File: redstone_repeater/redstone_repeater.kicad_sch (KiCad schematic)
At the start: 41 parts, among them J1 1x4_Pogo, J2 1x4_Pogo, J3 1x4_Pogo, J4 1x4_Pogo, J5 1x4_Pogo, J6 1x4_Pogo, J7 1x4_Pogo, J8 1x4_Pogo, J9 2.54mm_ProgrammingPin, Q1 BC108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

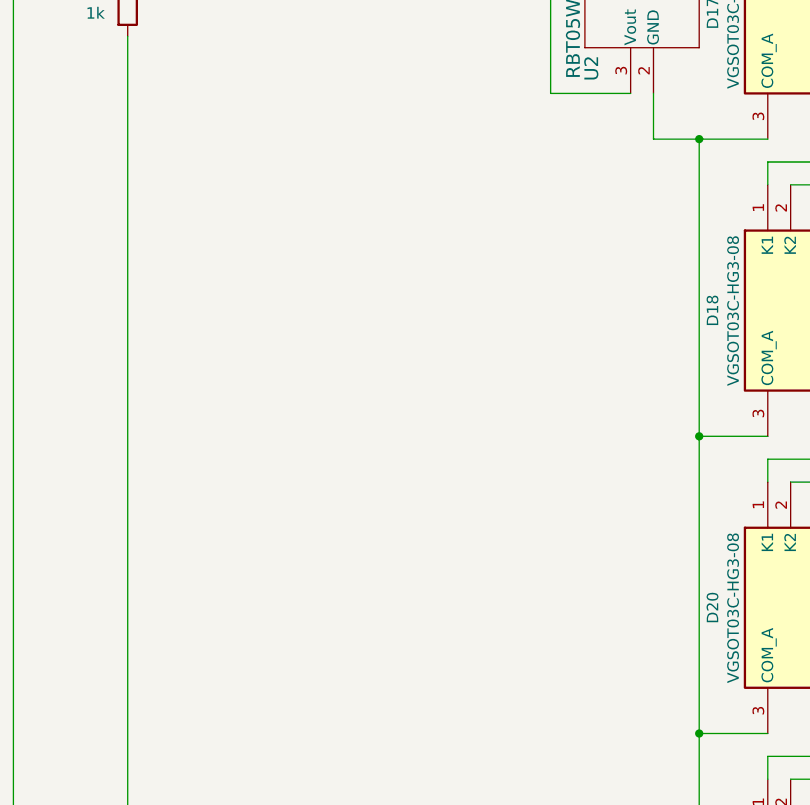
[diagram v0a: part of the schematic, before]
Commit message: add 4 way switch for repeater
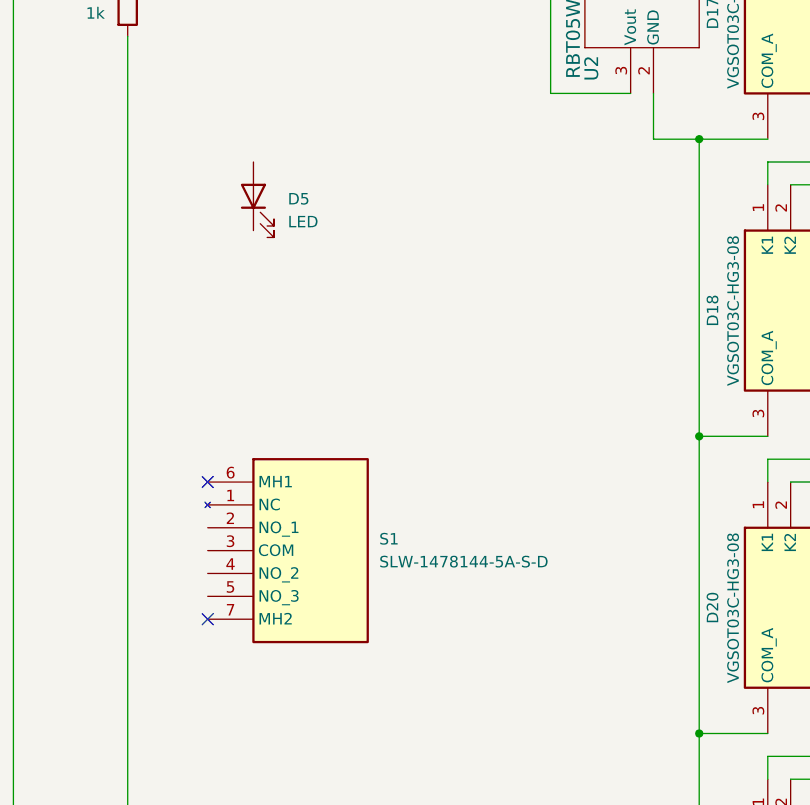
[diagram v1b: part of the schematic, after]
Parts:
- added D5: LED, LED_THT:LED_D3.0mm, symbol Device:LED
- added S1: SLW-1478144-5A-S-D, SLW14781445ASD, symbol SamacSys_Parts:SLW-1478144-5A-S-D
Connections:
- no-connect marks 34 -> 36
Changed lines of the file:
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@@
 	)
 	(no_connect
+		(at 187.96 100.33)
+	)
+	(no_connect
+		(at 187.96 115.57)
+	)
+	(no_connect
 		(at 128.27 157.48)
 	)
@@
 	)
 	(symbol
+		(lib_id "SamacSys_Parts:SLW-1478144-5A-S-D")
+		(at 187.96 100.33 0)
+		(unit 1)
+		(exclude_from_sim no)
+		(in_bom yes)
+		(on_board yes)
+		(dnp no)
+		(fields_autoplaced yes)
+		(property "Reference" "S1"
+			(at 207.01 106.6799 0)
+			(effects
+				(font
+					(size 1.27 1.27)
+				)
+				(justify left)
+			)
+		)
+		(property "Value" "SLW-1478144-5A-S-D"
+			(at 207.01 109.2199 0)
+			(effects
+				(font
+					(size 1.27 1.27)
+				)
+				(justify left)
+			)
+		)
+		(property "Footprint" "SLW14781445ASD"
+			(at 207.01 195.25 0)
+			(effects
+				(font
+					(size 1.27 1.27)
+				)
+				(justify left top)
+				(hide yes)
+			)
+		)
+		(property "Datasheet" "https://www.sameskydevices.com/product/resource/supplyframepdf/slw-1478144-5a-s-d.pdf"
+			(at 207.01 295.25 0)
+			(effects
+				(font
+					(size 1.27 1.27)
+				)
+				(justify left top)
+				(hide yes)
+			)
+		)
+		(property "Description" "14.7 x 8.1 x 4.4 mm, 5 mm Raised Slide Actuator, Through Hole, Slide Switch"
+			(at 187.96 100.33 0)
+			(effects
+				(font
+					(size 1.27 1.27)
+				)
+				(hide yes)
+			)
+		)
+		(property "Height" "10"
+			(at 207.01 495.25 0)
+			(effects
+				(font
+					(size 1.27 1.27)
+				)
+				(justify left top)
+				(hide yes)
+			)
+		)
+		(property "Manufacturer_Name" "Same Sky"
+			(at 207.01 595.25 0)
+			(effects
+				(font
+					(size 1.27 1.27)
+				)
+				(justify left top)
+				(hide yes)
+			)
+		)
+		(property "Manufacturer_Part_Number" "SLW-1478144-5A-S-D"
+			(at 207.01 695.25 0)
+			(effects
+				(font
+					(size 1.27 1.27)
+				)
+				(justify left top)
+				(hide yes)
+			)
+		)
+		(property "Mouser Part Number" ""
+			(at 207.01 795.25 0)
+			(effects
+				(font
+					(size 1.27 1.27)
+				)
+				(justify left top)
+				(hide yes)
+			)
+		)
+		(property "Mouser Price/Stock" ""
+			(at 207.01 895.25 0)
+			(effects
+				(font
+					(size 1.27 1.27)
+				)
+				(justify left top)
+				(hide yes)
+			)
+		)
+		(property "Arrow Part Number" ""
+			(at 207.01 995.25 0)
+			(effects
+				(font
+					(size 1.27 1.27)
+				)
+				(justify left top)
+				(hide yes)
+			)
+		)
+		(property "Arrow Price/Stock" ""
+			(at 207.01 1095.25 0)
+			(effects
+				(font
+					(size 1.27 1.27)
+				)
+				(justify left top)
+				(hide yes)
+			)
+		)
+		(pin "6"
+		)
+		(pin "2"
+		)
+		(pin "1"
+		)
+		(pin "4"
+		)
+		(pin "3"
+		)
+		(pin "7"
+		)
+		(pin "5"
+		)
+		(instances
+			(project ""
+				(path "/bc70a981-f687-4b66-9b14-62168cfa8164"
+					(reference "S1")
+					(unit 1)
+				)
+			)
+		)
+	)
+	(symbol
 		(lib_id "Connector_Generic_MountingPin:Conn_01x04_MountingPin")
 		(at 270.51 85.09 0)
@@
 					(unit 1)
 				)
+			)
+		)
+	)
+	(symbol
+		(lib_id "Device:LED")
+		(at 193.04 68.58 90)
+		(unit 1)
+		(exclude_from_sim no)
+		(in_bom yes)
+		(on_board yes)
+		(dnp no)
+		(fields_autoplaced yes)
+		(property "Reference" "D5"
+			(at 196.85 68.8974 90)
+			(effects
+				(font
+					(size 1.27 1.27)
+				)
+				(justify right)
+			)
+		)
+		(property "Value" "LED"
+			(at 196.85 71.4374 90)
+			(effects
+				(font
+					(size 1.27 1.27)
+				)
+				(justify right)
+			)
+		)
+		(property "Footprint" "LED_THT:LED_D3.0mm"
+			(at 193.04 68.58 0)
+			(effects
+				(font
+					(size 1.27 1.27)
+				)
+				(hide yes)
+			)
+		)
+		(property "Datasheet" "~"
+			(at 193.04 68.58 0)
+			(effects
+				(font
+					(size 1.27 1.27)
+				)
+				(hide yes)
+			)
+		)
+		(property "Description" "Light emitting diode"
+			(at 193.04 68.58 0)
+			(effects
+				(font
+					(size 1.27 1.27)
+				)
+				(hide yes)
+			)
+		)
+		(property "Sim.Pins" "1=K 2=A"
+			(at 193.04 68.58 0)
+			(effects
+				(font
+					(size 1.27 1.27)
+				)
+				(hide yes)
+			)
+		)
+		(pin "2"
+		)
+		(pin "1"
+		)
+		(instances
+			(project ""
+				(path "/bc70a981-f687-4b66-9b14-62168cfa8164"
+					(reference "D5")
+					(unit 1)
+				)

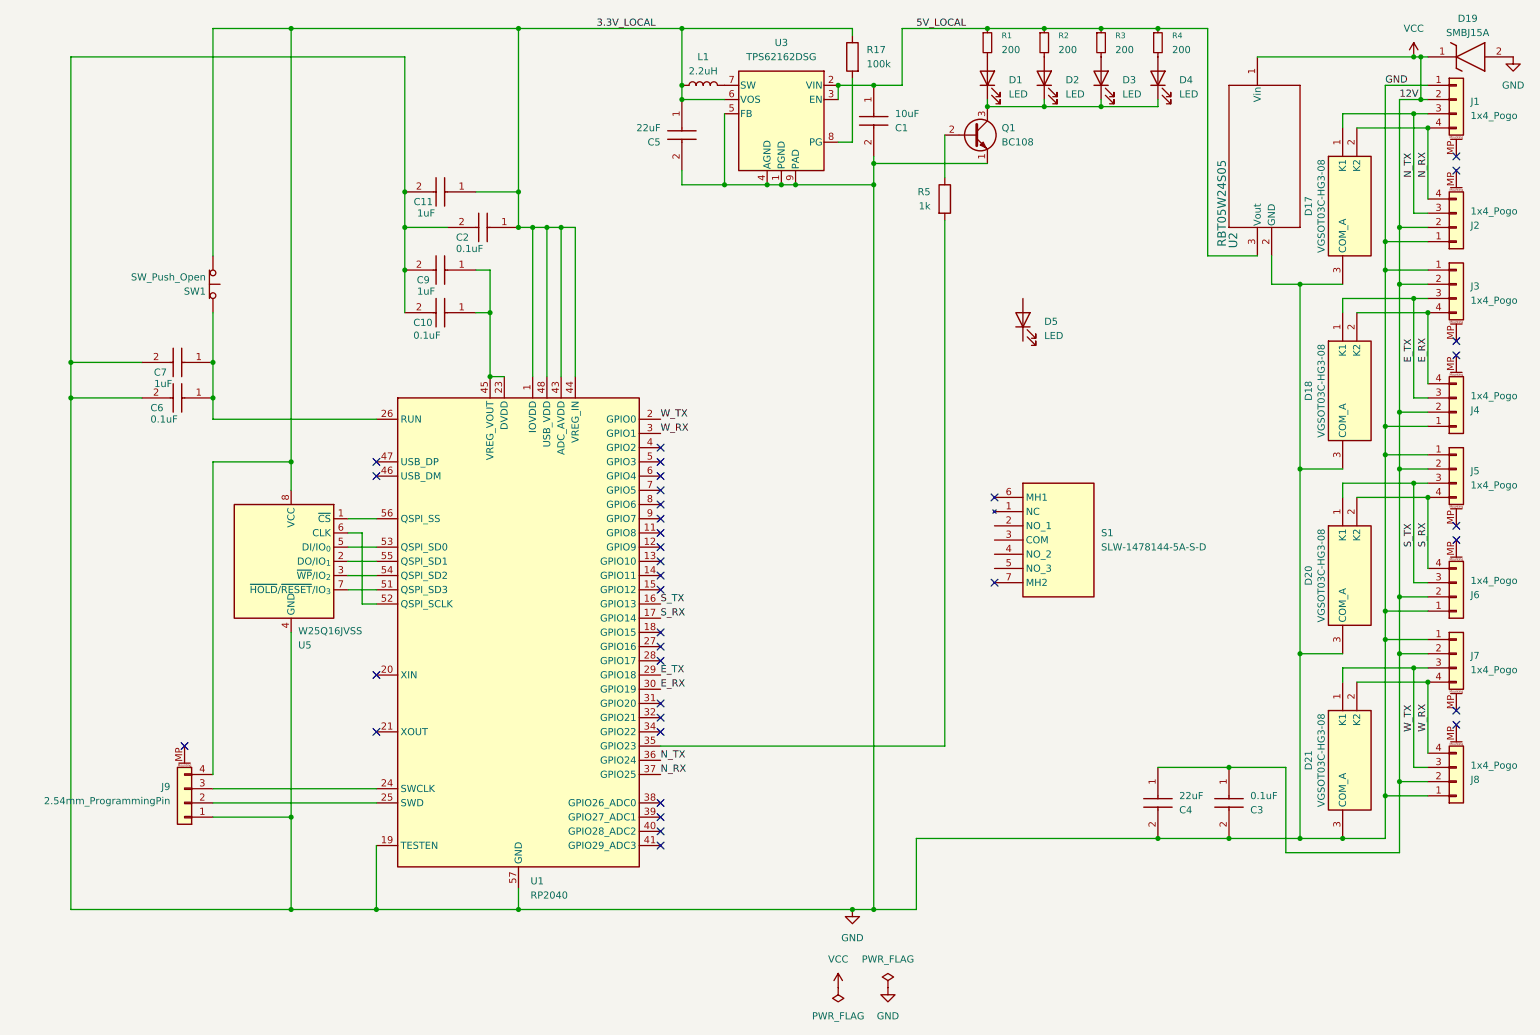
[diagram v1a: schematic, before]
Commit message: add four individually controlled leds for repeater, small adjustments for redstone dust
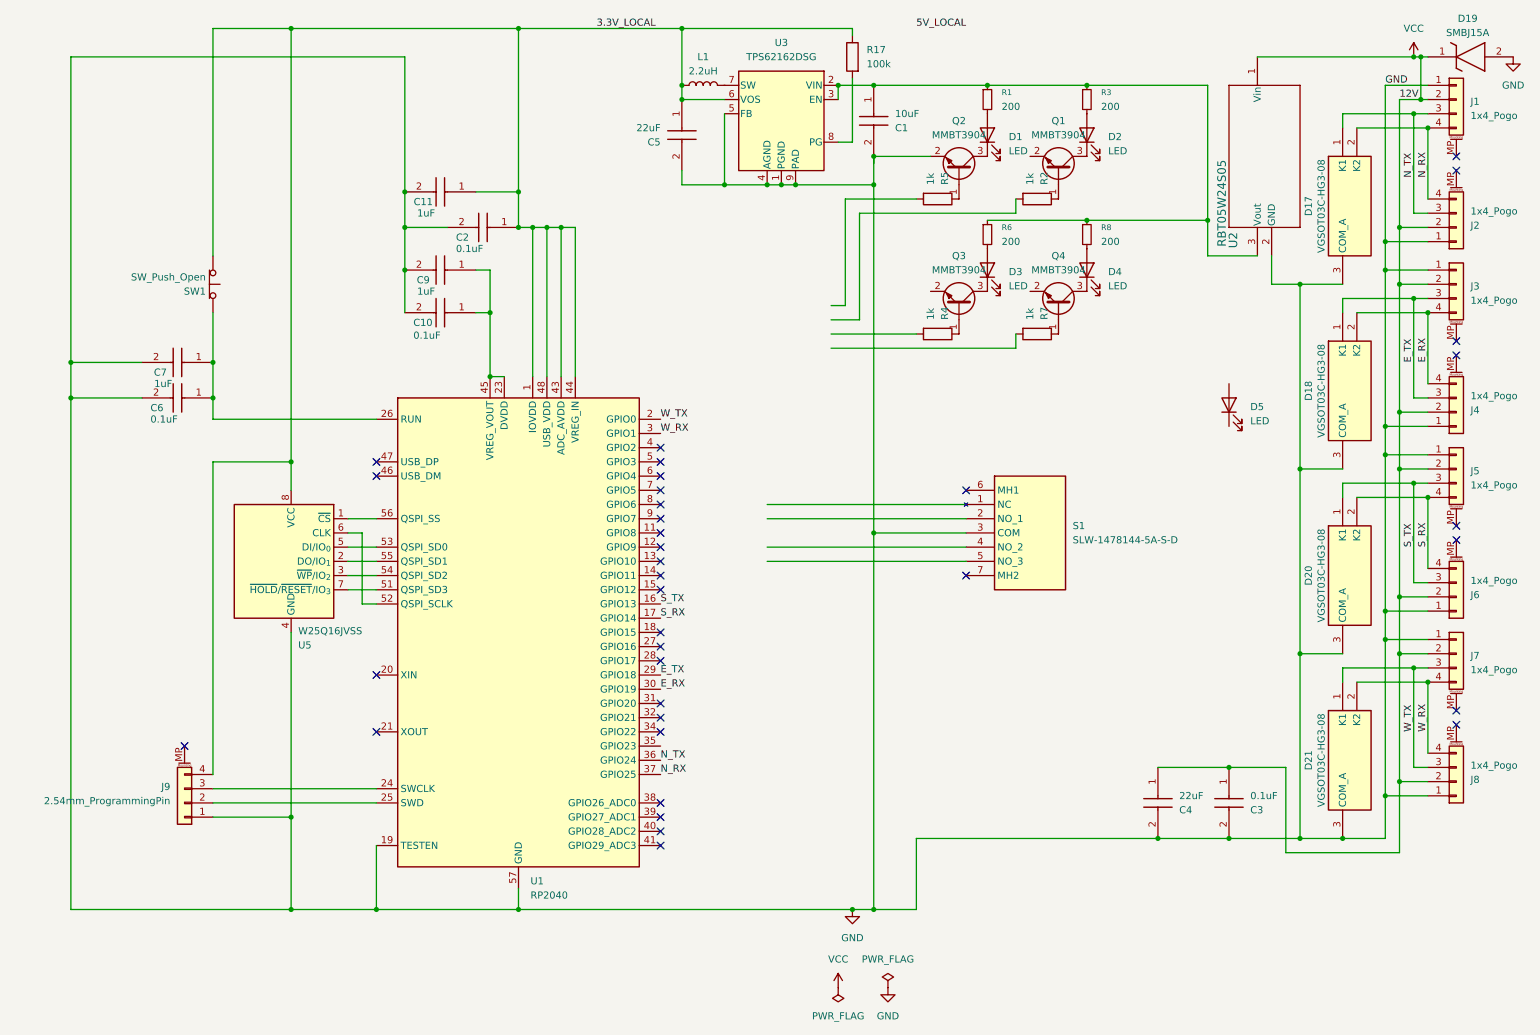
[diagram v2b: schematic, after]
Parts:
- removed Q1: BC108, Package_TO_SOT_THT:TO-18-3, symbol Transistor_BJT:BC108
- removed R2, R4: 200, SamacSys_Parts:CRCW1210200RJNEAIF, symbol Device:R_Small
- added Q1, Q2, Q3, Q4: MMBT3904, Package_TO_SOT_SMD:SOT-23, symbol Transistor_BJT:MMBT3904
- added R2, R4, R7: 1k, SamacSys_Parts:ERJ-UP6D1001V, symbol Device:R
- added R6, R8: 200, SamacSys_Parts:CRCW1210200RJNEAIF, symbol Device:R_Small
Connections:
- net 5V_LOCAL: no longer C1.1, R1.1, R3.1, U2.3 (Vout), U3.2 (VIN), U3.3 (EN)
- net GND: now also S1.3 (COM), Q2.2 (E)
- net at R3.2: now also D2.2 (A); no longer D3.2 (A)
- net at D4.2 (A): now also R8.2
- net at R5.1: now also Q2.1 (B)
- net at R5.2: no longer U1.35 (GPIO23)
- new net: D4.1 (K), Q4.3 (C)
- new net: Q4.1 (B), R7.1
- new net: C1.1, R1.1, R3.1, R6.1, R8.1, U2.3 (Vout), U3.2 (VIN), U3.3 (EN)
- new net: Q3.1 (B), R4.1
- new net: Q1.1 (B), R2.1
- new net: D2.1 (K), Q1.3 (C)
- new net: D3.1 (K), Q3.3 (C)
- new net: D3.2 (A), R6.2
- new net: D1.1 (K), Q2.3 (C)
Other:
- moved on the sheet: D1, D5, R1, R5, S1

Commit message: finalize schematic and finish layout of pcb
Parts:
- added Q5: MMBT3904, Package_TO_SOT_SMD:SOT-23, symbol Transistor_BJT:MMBT3904
- added R10: 200, SamacSys_Parts:CRCW1210200RJNEAIF, symbol Device:R_Small
- added R9: 1k, SamacSys_Parts:ERJ-UP6D1001V, symbol Device:R
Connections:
- net 5V_LOCAL: now also C1.1, R1.1, R3.1, R6.1, R8.1, U2.3 (Vout), U3.2 (VIN), U3.3 (EN), R10.1
- net E_RX: now also U1.17 (GPIO14); no longer U1.30 (GPIO19)
- net E_TX: now also U1.16 (GPIO13); no longer U1.29 (GPIO18)
- net GND: now also Q1.2 (E), Q3.2 (E), Q4.2 (E), Q5.2 (E)
- net N_RX: now also U1.36 (GPIO24); no longer U1.37 (GPIO25)
- net N_TX: now also U1.37 (GPIO25); no longer U1.36 (GPIO24)
- net S_RX: now also U1.14 (GPIO11); no longer U1.17 (GPIO14)
- net S_TX: now also U1.13 (GPIO10); no longer U1.16 (GPIO13)
- net at R7.2: now also U1.12 (GPIO9)
- net at R4.2: now also U1.11 (GPIO8)
- net at R5.2: now also U1.8 (GPIO6)
- net at S1.1 (NC): now also U1.4 (GPIO2)
- net at S1.2 (NO_1): now also U1.5 (GPIO3)
- net at S1.4 (NO_2): now also U1.6 (GPIO4)
- net at S1.5 (NO_3): now also U1.7 (GPIO5)
- net at R2.2: now also U1.9 (GPIO7)
- net at U1.15 (GPIO12): now also R9.2
- net at D5.1 (K): now also Q5.3 (C)
- net at D5.2 (A): now also R10.2
- new net: Q5.1 (B), R9.1
- no-connect marks 36 -> 28
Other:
- moved on the sheet: D2, D3, D4, D5, Q1, Q3, Q4, R2, R3, R4, R6, R7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

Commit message: finish wiring layout
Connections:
- net N_RX: now also U1.34 (GPIO22); no longer U1.36 (GPIO24)
- net N_TX: now also U1.35 (GPIO23); no longer U1.37 (GPIO25)
- net at Q1.1 (B): now also R5.1; no longer R2.1
- net at Q1.3 (C): now also D1.1 (K); no longer D2.1 (K)
- net at Q2.3 (C): now also D2.1 (K); no longer D1.1 (K)
- net at Q2.1 (B): now also R2.1; no longer R5.1
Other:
- moved on the sheet: Q1, Q2
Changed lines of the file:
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@@
 	)
 	(no_connect
-		(at 128.27 144.78)
+		(at 128.27 149.86)
 	)
 	(no_connect
@@
 	)
 	(no_connect
-		(at 128.27 142.24)
+		(at 128.27 147.32)
 	)
 	(no_connect
@@
 	)
 	(label "N_RX"
-		(at 128.27 147.32 0)
+		(at 128.27 142.24 0)
 		(effects
 			(font
@@
 	)
 	(label "N_TX"
-		(at 128.27 149.86 0)
+		(at 128.27 144.78 0)
 		(effects
 			(font
@@
 	(symbol
 		(lib_id "Transistor_BJT:MMBT3904")
-		(at 213.36 41.91 270)
+		(at 181.61 41.91 270)
 		(mirror x)
 		(unit 1)
@@
 		(fields_autoplaced yes)
 		(property "Reference" "Q1"
-			(at 213.36 33.02 90)
+			(at 181.61 33.02 90)
 			(effects
 				(font
@@
 		)
 		(property "Value" "MMBT3904"
-			(at 213.36 35.56 90)
+			(at 181.61 35.56 90)
 			(effects
 				(font
@@
 		)
 		(property "Footprint" "Package_TO_SOT_SMD:SOT-23"
-			(at 211.455 36.83 0)
+			(at 179.705 36.83 0)
 			(effects
 				(font
@@
 		)
 		(property "Datasheet" "https://www.onsemi.com/pdf/datasheet/pzt3904-d.pdf"
-			(at 213.36 41.91 0)
+			(at 181.61 41.91 0)
 			(effects
 				(font
@@
 		)
 		(property "Description" "0.2A Ic, 40V Vce, Small Signal NPN Transistor, SOT-23"
-			(at 213.36 41.91 0)
+			(at 181.61 41.91 0)
 			(effects
 				(font
@@
 	(symbol
 		(lib_id "Transistor_BJT:MMBT3904")
-		(at 181.61 41.91 270)
+		(at 213.36 41.91 270)
 		(mirror x)
 		(unit 1)
@@
 		(fields_autoplaced yes)
 		(property "Reference" "Q2"
-			(at 181.61 33.02 90)
+			(at 213.36 33.02 90)
 			(effects
 				(font
@@
 		)
 		(property "Value" "MMBT3904"
-			(at 181.61 35.56 90)
+			(at 213.36 35.56 90)
 			(effects
 				(font
@@
 		)
 		(property "Footprint" "Package_TO_SOT_SMD:SOT-23"
-			(at 179.705 36.83 0)
+			(at 211.455 36.83 0)
 			(effects
 				(font
@@
 		)
 		(property "Datasheet" "https://www.onsemi.com/pdf/datasheet/pzt3904-d.pdf"
-			(at 181.61 41.91 0)
+			(at 213.36 41.91 0)
 			(effects
 				(font
@@
 		)
 		(property "Description" "0.2A Ic, 40V Vce, Small Signal NPN Transistor, SOT-23"
-			(at 181.61 41.91 0)
+			(at 213.36 41.91 0)
 			(effects
 				(font
